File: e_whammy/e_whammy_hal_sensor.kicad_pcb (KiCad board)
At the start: 2 copper layers, 17 x 26 mm, 12 parts, among them J1 I/O connector, U1 HT7550-1, U2 DRV5056

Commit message: refinements
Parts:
- moved C3 1.91 mm to (120.3, 112.0), turned to -90 degrees
- moved C2 1.48 mm to (121.3, 113.8), turned to 180 degrees
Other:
- board text added: "OUT"
- board text added: "V+"
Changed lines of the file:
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@@
 	(footprint "Capacitor_SMD:C_0402_1005Metric"
 		(layer "F.Cu")
-		(at 120.98 110.2)
+		(at 120.3 111.98 -90)
 		(descr "Capacitor SMD 0402 (1005 Metric), square (rectangular) end terminal, IPC-7351 nominal, (Body size source: IPC-SM-782 page 76, https://www.pcb-3d.com/wordpress/wp-content/uploads/ipc-sm-782a_amendment_1_and_2.pdf), generated with kicad-footprint-generator")
 		(tags "capacitor")
 		(property "Reference" "C3"
-			(at 0 -1.16 0)
+			(at 0 -1.16 90)
 			(layer "F.SilkS")
 			(hide yes)
@@
 		)
 		(property "Value" "100nF"
-			(at 0 1.16 0)
+			(at 0 1.16 90)
 			(layer "F.Fab")
 			(effects
@@
 		)
 		(property "Datasheet" "~"
-			(at 0 0 0)
+			(at 0 0 90)
 			(layer "F.Fab")
 			(hide yes)
@@
 		)
 		(property "Description" ""
-			(at 0 0 0)
+			(at 0 0 90)
 			(layer "F.Fab")
 			(hide yes)
@@
 		)
 		(property "LCSC" "C307331"
-			(at 0 0 0)
+			(at 0 0 270)
 			(unlocked yes)
 			(layer "F.Fab")
@@
 		(attr smd)
 		(fp_line
+			(start -0.107836 0.36)
+			(end 0.107836 0.36)
+			(stroke
+				(width 0.12)
+				(type solid)
+			)
+			(layer "F.SilkS")
+		)
+		(fp_line
 			(start -0.107836 -0.36)
 			(end 0.107836 -0.36)
@@
 		)
 		(fp_line
-			(start -0.107836 0.36)
-			(end 0.107836 0.36)
-			(stroke
-				(width 0.12)
-				(type solid)
-			)
-			(layer "F.SilkS")
+			(start -0.91 0.46)
+			(end -0.91 -0.46)
+			(stroke
+				(width 0.05)
+				(type solid)
+			)
+			(layer "F.CrtYd")
+		)
+		(fp_line
+			(start 0.91 0.46)
+			(end -0.91 0.46)
+			(stroke
+				(width 0.05)
+				(type solid)
+			)
+			(layer "F.CrtYd")
 		)
 		(fp_line
@@
 		)
 		(fp_line
-			(start -0.91 0.46)
-			(end -0.91 -0.46)
-			(stroke
-				(width 0.05)
-				(type solid)
-			)
-			(layer "F.CrtYd")
-		)
-		(fp_line
 			(start 0.91 -0.46)
 			(end 0.91 0.46)
@@
 		)
 		(fp_line
-			(start 0.91 0.46)
-			(end -0.91 0.46)
-			(stroke
-				(width 0.05)
-				(type solid)
-			)
-			(layer "F.CrtYd")
+			(start -0.5 0.25)
+			(end -0.5 -0.25)
+			(stroke
+				(width 0.1)
+				(type solid)
+			)
+			(layer "F.Fab")
+		)
+		(fp_line
+			(start 0.5 0.25)
+			(end -0.5 0.25)
+			(stroke
+				(width 0.1)
+				(type solid)
+			)
+			(layer "F.Fab")
 		)
 		(fp_line
@@
 		)
 		(fp_line
-			(start -0.5 0.25)
-			(end -0.5 -0.25)
-			(stroke
-				(width 0.1)
-				(type solid)
-			)
-			(layer "F.Fab")
-		)
-		(fp_line
 			(start 0.5 -0.25)
 			(end 0.5 0.25)
@@
 			(layer "F.Fab")
 		)
-		(fp_line
-			(start 0.5 0.25)
-			(end -0.5 0.25)
-			(stroke
-				(width 0.1)
-				(type solid)
-			)
-			(layer "F.Fab")
-		)
 		(fp_text user "${REFERENCE}"
-			(at 0 0 0)
+			(at 0 0 90)
 			(layer "F.Fab")
 			(effects
@@
 		)
 		(pad "1" smd roundrect
-			(at -0.48 0)
+			(at -0.48 0 270)
 			(size 0.56 0.62)
 			(layers "F.Cu" "F.Mask" "F.Paste")
@@
 		)
 		(pad "2" smd roundrect
-			(at 0.48 0)
+			(at 0.48 0 270)
 			(size 0.56 0.62)
 			(layers "F.Cu" "F.Mask" "F.Paste")
@@
 	(footprint "Capacitor_SMD:C_0603_1608Metric"
 		(layer "F.Cu")
-		(at 120.9 112.375 -90)
+		(at 121.3 113.8 180)
 		(descr "Capacitor SMD 0603 (1608 Metric), square (rectangular) end terminal, IPC-7351 nominal, (Body size source: IPC-SM-782 page 76, https://www.pcb-3d.com/wordpress/wp-content/uploads/ipc-sm-782a_amendment_1_and_2.pdf), generated with kicad-footprint-generator")
 		(tags "capacitor")
 		(property "Reference" "C2"
-			(at 0 -1.43 90)
+			(at 0 -1.43 0)
 			(layer "F.SilkS")
 			(hide yes)
@@
 		)
 		(property "Value" "10uF"
-			(at 0 1.43 90)
+			(at 0 1.43 0)
 			(layer "F.Fab")
 			(effects
@@
 		)
 		(property "Datasheet" "~"
-			(at 0 0 90)
+			(at 0 0 0)
 			(layer "F.Fab")
 			(hide yes)
@@
 		)
 		(property "Description" ""
-			(at 0 0 90)
+			(at 0 0 0)
 			(layer "F.Fab")
 			(hide yes)
@@
 		)
 		(property "LCSC" "C96446"
-			(at 0 0 270)
+			(at 0 0 180)
 			(unlocked yes)
 			(layer "F.Fab")
@@
 		)
 		(fp_line
+			(start 1.48 0.73)
+			(end -1.48 0.73)
+			(stroke
+				(width 0.05)
+				(type solid)
+			)
+			(layer "F.CrtYd")
+		)
+		(fp_line
+			(start 1.48 -0.73)
+			(end 1.48 0.73)
+			(stroke
+				(width 0.05)
+				(type solid)
+			)
+			(layer "F.CrtYd")
+		)
+		(fp_line
 			(start -1.48 0.73)
 			(end -1.48 -0.73)
@@
 		)
 		(fp_line
-			(start 1.48 0.73)
-			(end -1.48 0.73)
-			(stroke
-				(width 0.05)
-				(type solid)
-			)
-			(layer "F.CrtYd")
-		)
-		(fp_line
 			(start -1.48 -0.73)
 			(end 1.48 -0.73)
@@
 		)
 		(fp_line
-			(start 1.48 -0.73)
-			(end 1.48 0.73)
-			(stroke
-				(width 0.05)
-				(type solid)
-			)
-			(layer "F.CrtYd")
+			(start 0.8 0.4)
+			(end -0.8 0.4)
+			(stroke
+				(width 0.1)
+				(type solid)
+			)
+			(layer "F.Fab")
+		)
+		(fp_line
+			(start 0.8 -0.4)
+			(end 0.8 0.4)
+			(stroke
+				(width 0.1)
+				(type solid)
+			)
+			(layer "F.Fab")
 		)
 		(fp_line
@@
 		)
 		(fp_line
-			(start 0.8 0.4)
-			(end -0.8 0.4)
-			(stroke
-				(width 0.1)
-				(type solid)
-			)
-			(layer "F.Fab")
-		)
-		(fp_line
 			(start -0.8 -0.4)
 			(end 0.8 -0.4)
@@
 			(layer "F.Fab")
 		)
-		(fp_line
-			(start 0.8 -0.4)
-			(end 0.8 0.4)
-			(stroke
-				(width 0.1)
-				(type solid)
-			)
-			(layer "F.Fab")
-		)
 		(fp_text user "${REFERENCE}"
-			(at 0 0 90)
+			(at 0 0 0)
 			(layer "F.Fab")
 			(effects
@@
 		)
 		(pad "1" smd roundrect
-			(at -0.775 0 270)
+			(at -0.775 0 180)
 			(size 0.9 0.95)
 			(layers "F.Cu" "F.Mask" "F.Paste")
@@
 		)
 		(pad "2" smd roundrect
-			(at 0.775 0 270)
+			(at 0.775 0 180)
 			(size 0.9 0.95)
 			(layers "F.Cu" "F.Mask" "F.Paste")
@@
 		(layer "F.SilkS")
 	)
+	(gr_poly
+		(pts
+			(xy 117.5 109.75) (xy 118.5 109.75) (xy 118 110.5)
+		)
+		(stroke
+			(width 0.15)
+			(type solid)
+		)
+		(fill yes)
+		(layer "F.SilkS")
+	)
 	(gr_line
 		(start 118 98)
@@
 		)
 		(layer "Edge.Cuts")
+	)
+	(gr_text "V+"
+		(at 119.84 110.56 0)
+		(layer "F.SilkS")
+		(effects
+			(font
+				(size 0.8 0.8)
+				(thickness 0.15)
+			)
+			(justify left bottom)
+		)
 	)
 	(gr_text "HE v1.0"
@@
 		)
 	)
+	(gr_text "OUT"
+		(at 114.095 110.56 0)
+		(layer "F.SilkS")
+		(effects
+			(font
+				(size 0.8 0.8)
+				(thickness 0.15)
+			)
+			(justify left bottom)
+		)
+	)
 	(segment
 		(start 124 111.4)
@@
 	)
 	(segment
-		(start 122.8625 112.35)
-		(end 122.8625 111.8875)
+		(start 119.8625 111.0625)
+		(end 120.3 111.5)
 		(width 0.5)
 		(layer "F.Cu")
@@
 	(segment
 		(start 118.95 111.0625)
-		(end 120.8625 111.0625)
+		(end 119.8625 111.0625)
 		(width 0.5)
 		(layer "F.Cu")
@@
 	)
 	(segment
-		(start 122.8625 111.8875)
-		(end 122.575 111.6)
+		(start 122.0125 111.5)
+		(end 122.8625 112.35)
 		(width 0.5)
 		(layer "F.Cu")
@@
 	)
 	(segment
-		(start 120.9 111.1)
-		(end 120.5 110.7)
-		(width 0.5)
-		(layer "F.Cu")
-		(net 3)
-	)
-	(segment
-		(start 120.9 111.1)
-		(end 120.9 111.6)
+		(start 122.8625 113.0125)
+		(end 122.075 113.8)
 		(width 0.5)
 		(layer "F.Cu")
@@
 	)
 	(segment
+		(start 120.3 111.5)
+		(end 122.0125 111.5)
+		(width 0.5)
+		(layer "F.Cu")
+		(net 3)
+	)
+	(segment
 		(start 118.95 111.0625)
 		(end 118.95 113.437678)
@@
 	)
 	(segment
-		(start 120.5 110.7)
-		(end 120.5 110.2)
-		(width 0.5)
-		(layer "F.Cu")
-		(net 3)
-	)
-	(segment
-		(start 122.575 111.6)
-		(end 120.9 111.6)
-		(width 0.5)
-		(layer "F.Cu")
-		(net 3)
-	)
-	(segment
-		(start 120.8625 111.0625)
-		(end 120.9 111.1)
+		(start 122.8625 112.35)
+		(end 122.8625 113.0125)
 		(width 0.5)
 		(layer "F.Cu")
@@
 		(min_thickness 0.254)
 		(filled_areas_thickness no)
-		(fill
+		(fill yes
 			(thermal_gap 0.508)
 			(thermal_bridge_width 0.508)

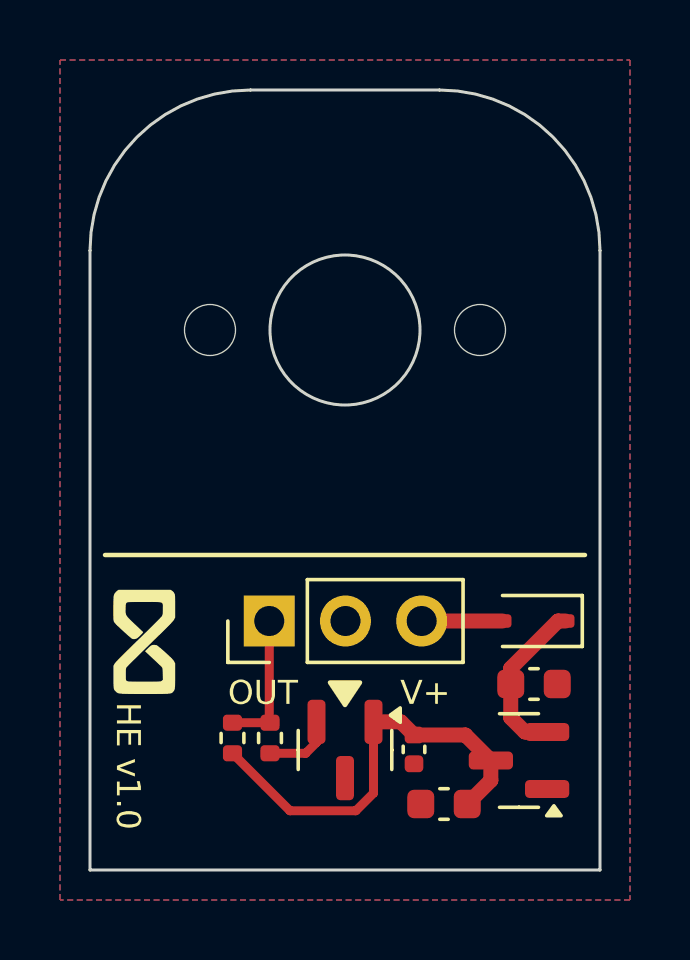
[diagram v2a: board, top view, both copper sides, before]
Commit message: Separate control and sensor
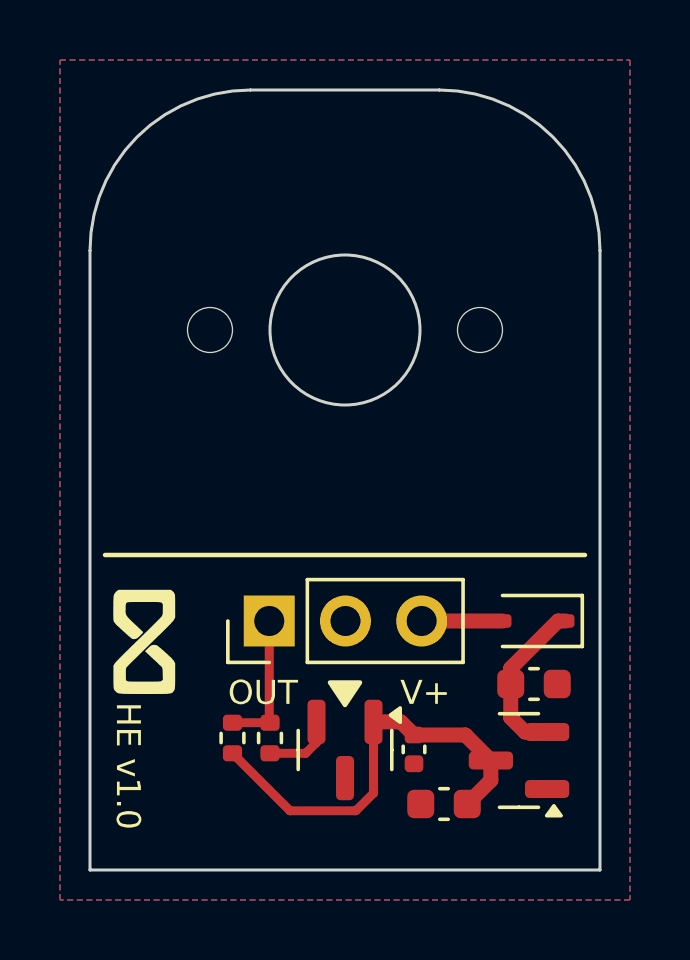
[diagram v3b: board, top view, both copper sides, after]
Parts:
- REF** (x2): value hole_1.7mm -> hole_1.4mm; footprint cycfi_library:hole_1.7mm -> cycfi_library:hole_1.4mm
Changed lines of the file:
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@@
 		)
 	)
-	(footprint "cycfi_library:hole_1.7mm"
+	(footprint "cycfi_library:hole_1.4mm"
 		(layer "F.Cu")
 		(at 122.5 98)
@@
 			)
 		)
-		(property "Value" "hole_1.7mm"
+		(property "Value" "hole_1.4mm"
 			(at 0 3.2 0)
 			(layer "F.Fab")
@@
 		(pad "" np_thru_hole circle
 			(at 0 0)
-			(size 1.7 1.7)
-			(drill 1.7)
+			(size 1.4 1.4)
+			(drill 1.5)
 			(layers "*.Cu" "*.Mask")
 		)
@@
 		)
 	)
-	(footprint "cycfi_library:hole_1.7mm"
+	(footprint "cycfi_library:hole_1.4mm"
 		(layer "F.Cu")
 		(at 113.5 98)
@@
 			)
 		)
-		(property "Value" "hole_1.7mm"
+		(property "Value" "hole_1.4mm"
 			(at 0 3.2 0)
 			(layer "F.Fab")
@@
 		(pad "" np_thru_hole circle
 			(at 0 0)
-			(size 1.7 1.7)
-			(drill 1.7)
+			(size 1.4 1.4)
+			(drill 1.5)
 			(layers "*.Cu" "*.Mask")
 		)

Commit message: Updated circuit matching the E-Whammy control design.
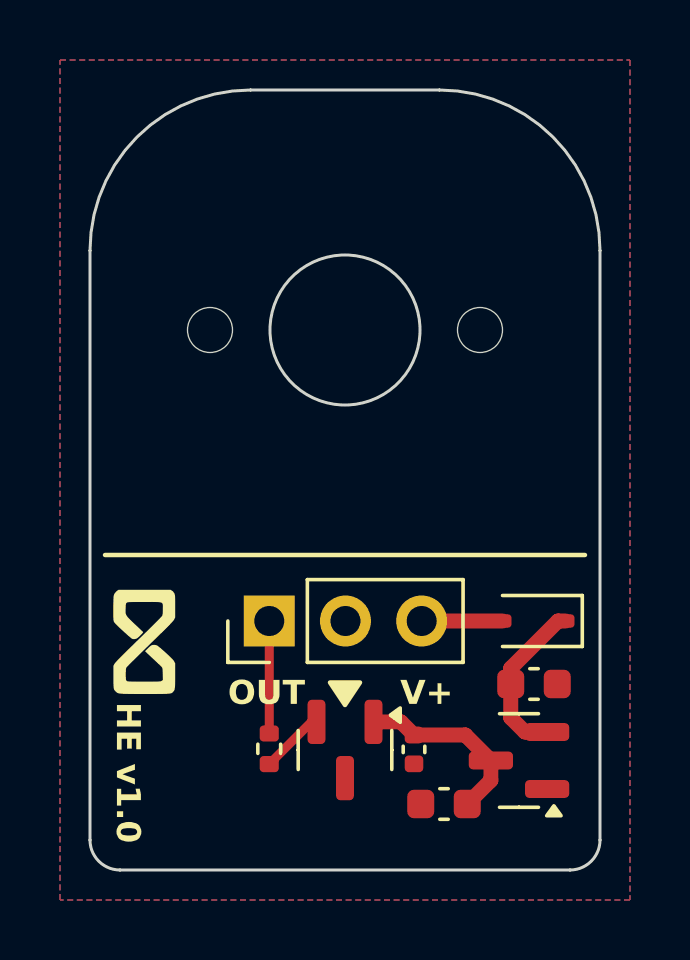
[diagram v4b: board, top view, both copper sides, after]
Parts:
- removed R3, R5: 10K, Resistor_SMD:R_0402_1005Metric
- added R1: 47K, Resistor_SMD:R_0402_1005Metric, F.Cu at (115.5, 112.0)
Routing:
- net 5v: track 14.3 -> 6.22 mm
- net OUT: track 4.65 -> 3.75 mm
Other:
- outline, holes or cut-outs redrawn

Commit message: Tighter tolerance
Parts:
- REF** (x2): value hole_1.4mm -> hole_1.45mm; footprint cycfi_library:hole_1.4mm -> cycfi_library:hole_1.45mm
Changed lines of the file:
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@@
 		)
 	)
-	(footprint "cycfi_library:hole_1.4mm"
+	(footprint "cycfi_library:hole_1.45mm"
 		(layer "F.Cu")
 		(at 122.5 98)
@@
 			)
 		)
-		(property "Value" "hole_1.4mm"
+		(property "Value" "hole_1.45mm"
 			(at 0 3.2 0)
 			(layer "F.Fab")
@@
 			)
 		)
-		(attr board_only exclude_from_pos_files exclude_from_bom)
+		(attr exclude_from_pos_files exclude_from_bom)
 		(fp_circle
 			(center 0 0)
@@
 		(pad "" np_thru_hole circle
 			(at 0 0)
-			(size 1.4 1.4)
+			(size 1.45 1.45)
 			(drill 1.5)
 			(layers "*.Cu" "*.Mask")
@@
 		)
 	)
-	(footprint "cycfi_library:hole_1.4mm"
+	(footprint "cycfi_library:hole_1.45mm"
 		(layer "F.Cu")
 		(at 113.5 98)
@@
 			)
 		)
-		(property "Value" "hole_1.4mm"
+		(property "Value" "hole_1.45mm"
 			(at 0 3.2 0)
 			(layer "F.Fab")
@@
 			)
 		)
-		(attr board_only exclude_from_pos_files exclude_from_bom)
+		(attr exclude_from_pos_files exclude_from_bom)
 		(fp_circle
 			(center 0 0)
@@
 		(pad "" np_thru_hole circle
 			(at 0 0)
-			(size 1.4 1.4)
+			(size 1.45 1.45)
 			(drill 1.5)
 			(layers "*.Cu" "*.Mask")

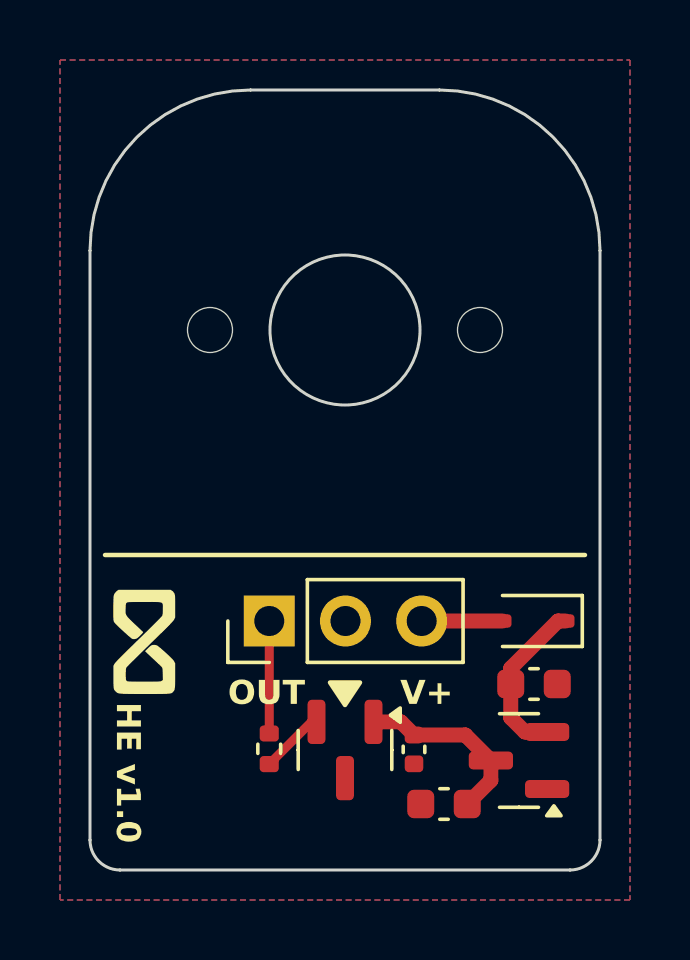
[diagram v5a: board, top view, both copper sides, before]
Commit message: E-Whammy update: bug fixes and refinements
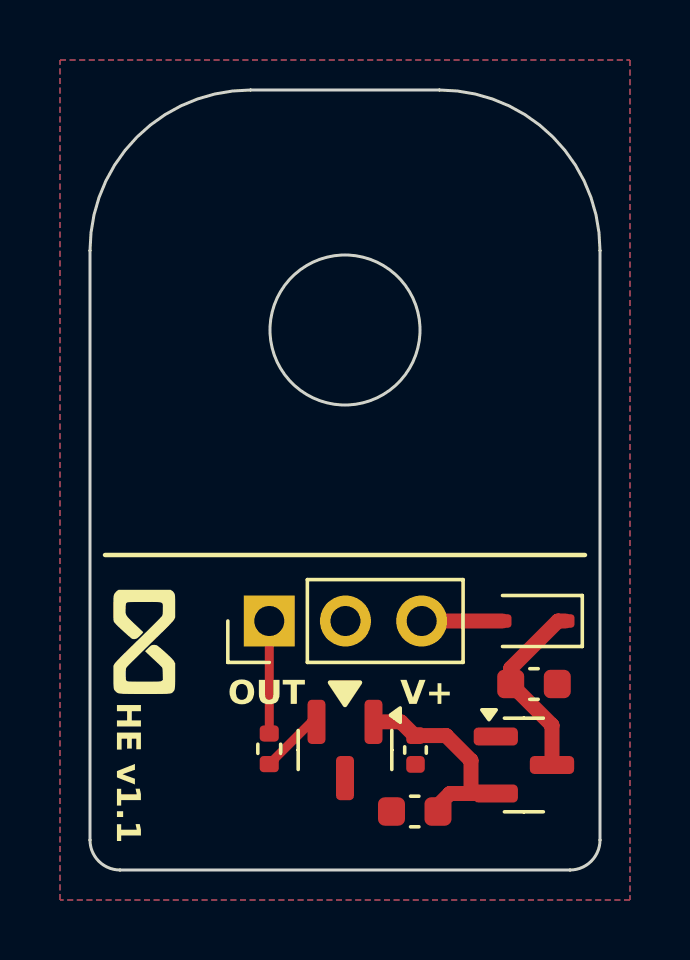
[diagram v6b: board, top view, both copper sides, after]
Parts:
- removed REF** (x2): hole_1.45mm, cycfi_library:hole_1.45mm
- U1: footprint Package_TO_SOT_SMD:SOT-23 -> cycfi_library:SOT-23-132
- moved C2 1.01 mm to (120.3, 114.0)
- moved U1 0.22 mm to (124.0, 112.5), turned to 0 degrees
- moved C3 0.05 mm to (120.3, 112.0)
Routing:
- net Net-(D1-K): track 5.54 -> 6.27 mm
- net 5v: track 6.22 -> 6.92 mm
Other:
- board text added: "HE v1.1"
- board text removed: "HE v1.0"

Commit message: The alignment holes are missing!
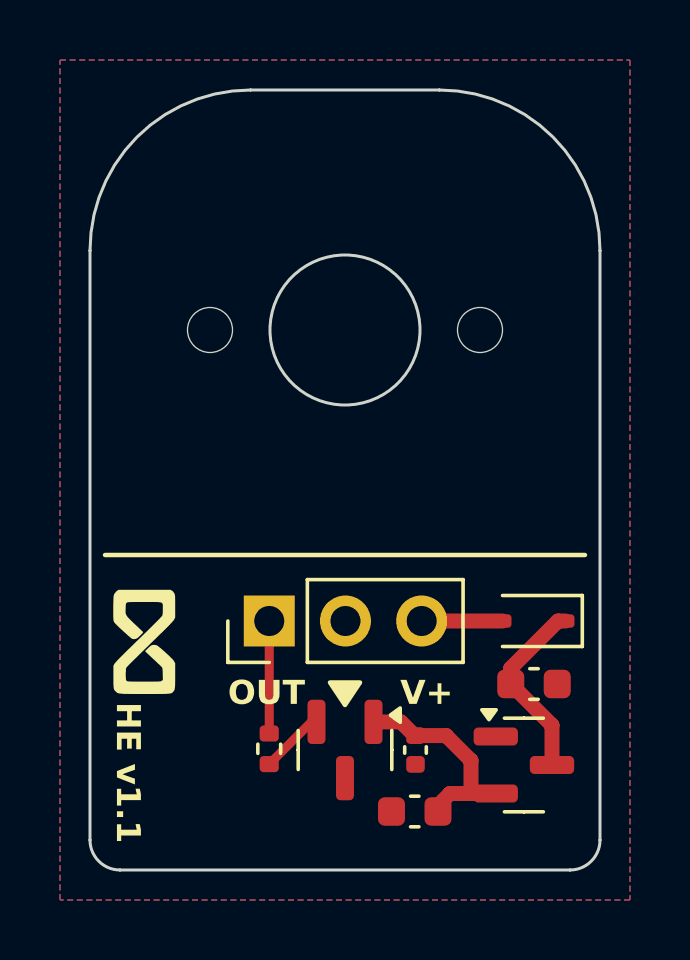
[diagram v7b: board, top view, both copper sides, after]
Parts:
- added ?: , , F.Cu at (113.5, 98.0)
- added ?: , , F.Cu at (122.5, 98.0)
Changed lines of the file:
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@@
 		)
+	)
+	(footprint ""
+		(layer "F.Cu")
+		(at 113.5 98)
+		(property "Reference" ""
+			(at 0 0 0)
+			(layer "F.SilkS")
+			(effects
+				(font
+					(size 1.27 1.27)
+					(thickness 0.15)
+				)
+			)
+		)
+		(property "Value" ""
+			(at 0 0 0)
+			(layer "F.Fab")
+			(effects
+				(font
+					(size 1.27 1.27)
+					(thickness 0.15)
+				)
+			)
+		)
+		(property "Datasheet" ""
+			(at 0 0 0)
+			(layer "F.Fab")
+			(hide yes)
+			(effects
+				(font
+					(size 1.27 1.27)
+					(thickness 0.15)
+				)
+			)
+		)
+		(property "Description" ""
+			(at 0 0 0)
+			(layer "F.Fab")
+			(hide yes)
+			(effects
+				(font
+					(size 1.27 1.27)
+					(thickness 0.15)
+				)
+			)
+		)
+		(attr board_only)
+		(pad "" np_thru_hole circle
+			(at 0 0)
+			(size 1.45 1.45)
+			(drill 1.5)
+			(layers "*.Cu" "*.Mask")
+		)
+		(embedded_fonts no)
 	)
 	(footprint "cycfi_library:infinity_logo_4mm"
@@
 		)
 	)
+	(footprint ""
+		(layer "F.Cu")
+		(at 122.5 98)
+		(property "Reference" ""
+			(at 0 0 0)
+			(layer "F.SilkS")
+			(effects
+				(font
+					(size 1.27 1.27)
+					(thickness 0.15)
+				)
+			)
+		)
+		(property "Value" ""
+			(at 0 0 0)
+			(layer "F.Fab")
+			(effects
+				(font
+					(size 1.27 1.27)
+					(thickness 0.15)
+				)
+			)
+		)
+		(property "Datasheet" ""
+			(at 0 0 0)
+			(layer "F.Fab")
+			(hide yes)
+			(effects
+				(font
+					(size 1.27 1.27)
+					(thickness 0.15)
+				)
+			)
+		)
+		(property "Description" ""
+			(at 0 0 0)
+			(layer "F.Fab")
+			(hide yes)
+			(effects
+				(font
+					(size 1.27 1.27)
+					(thickness 0.15)
+				)
+			)
+		)
+		(attr board_only)
+		(pad "" np_thru_hole circle
+			(at 0 0)
+			(size 1.45 1.45)
+			(drill 1.5)
+			(layers "*.Cu" "*.Mask")
+		)
+		(embedded_fonts no)
+	)
 	(footprint "Capacitor_SMD:C_0603_1608Metric"
 		(layer "F.Cu")
@@
 	)
 	(gr_line
-		(start 126.5 120)
+		(start 126.5 116)
 		(end 126.5 95.35)
 		(stroke
@@
 	)
 	(gr_line
-		(start 109.5 120)
-		(end 126.5 120)
+		(start 109.5 116)
+		(end 126.5 116)
 		(stroke
 			(width 0.05)
@@
 	(gr_line
 		(start 109.5 95.349981)
-		(end 109.5 120)
-		(stroke
-			(width 0.05)
+		(end 109.5 116)
+		(stroke
+			(width 0.05)
